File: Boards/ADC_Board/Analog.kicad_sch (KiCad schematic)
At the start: 62 parts, among them J1 Load Cell A, J2 Load Cell B, J3 Load Cell C, J4 Thermocouple A, J5 Cold Juntion Thermistor, J6 Thermocouple A, J7 Thermocouple A, U1 ADS124S08IRHBR

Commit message: Somewhat done servo+adc boards
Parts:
- added C27, C31, C35: 100n, symbol Device:C
- added J15, J17, J19: MIPA_A, symbol Connector_Generic:Conn_01x03
- added R28, R34, R39: 2K, symbol Device:R
- C17: renamed from C3; value XX -> 100n
- C19: renamed from C1; value C -> 200n
- C20: renamed from C4; value XX -> 100n
- C21: renamed from C5; value XX -> 100n
- C22: renamed from C2; value C -> 200n
- C23: renamed from C16; value XX -> 100n
- C24: renamed from C17; value XX -> 100n
- C25: renamed from C22; value C -> 200n
- C26: renamed from C21; value XX -> 100n
- C28: renamed from C23; value XX -> 100n
- C29: renamed from C25; value C -> 200n
- C30: renamed from C24; value XX -> 100n
- C32: renamed from C26; value XX -> 100n
- C33: renamed from C28; value C -> 200n
- C34: renamed from C27; value XX -> 100n
- C36: renamed from C30; value XX -> 100n
- C37: renamed from C32; value C -> 200n
- C38: renamed from C31; value XX -> 100n
- C39: renamed from C36; value XX -> 100n
- C40: renamed from C38; value C -> 200n
- C41: renamed from C37; value XX -> 100n
- C42: renamed from C29; value C -> 100n
- J20: renamed from J6; value Thermocouple A -> Thermocouple B
- J21: renamed from J7; value Thermocouple A -> Thermocouple C
- R18: renamed from R1; value R -> 2K
- R19: renamed from R2; value R -> 2K
- R20: renamed from R3; value R -> 2K
- R22: renamed from R4; value R -> 2K
- R24: renamed from R5; value R -> 2K
- R27: renamed from R11; value R -> 2K
- R30: renamed from R13; value R -> 2K
- R33: renamed from R14; value R -> 2K
- R36: renamed from R15; value R -> 2K
- R37: renamed from R16; value R -> 2K
- R41: renamed from R21; value R -> 2K
- R42: renamed from R22; value R -> 2K
- R46: renamed from R26; value R -> 2K
- R47: renamed from R20; value R -> 2K
- R48: renamed from R33; value R -> 2K
- renumbered C33 to C15, C34 to C16, C35 to C18, J1 to J13, J2 to J14, J3 to J16, J4 to J18, J5 to J22, R25 to R21, R27 to R23, R28 to R25, R29 to R26, R30 to R29, R17 to R35, R18 to R38, R23 to R40, R24 to R43, R34 to R44, R19 to R45, R35 to R49, U1 to U5
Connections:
- net +5V: now also J15.3 (Pin_3), J17.3 (Pin_3), J19.3 (Pin_3)
- net GND: now also C27.2, C31.2, C35.2, J15.1 (Pin_1), J17.1 (Pin_1), J19.1 (Pin_1)
- new net: J17.2 (Pin_2), R34.1
- new net: J19.2 (Pin_2), R39.1
- new net: J15.2 (Pin_2), R28.1
- new net MIPA_A: C27.1, R28.2
- new net MIPA_B: C31.1, R34.2
- new net MIPA_C: C35.1, R39.2
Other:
- note added: "Filters have a -3dB point at 800Hz"
- note added: "MIPA Pres Sensors"

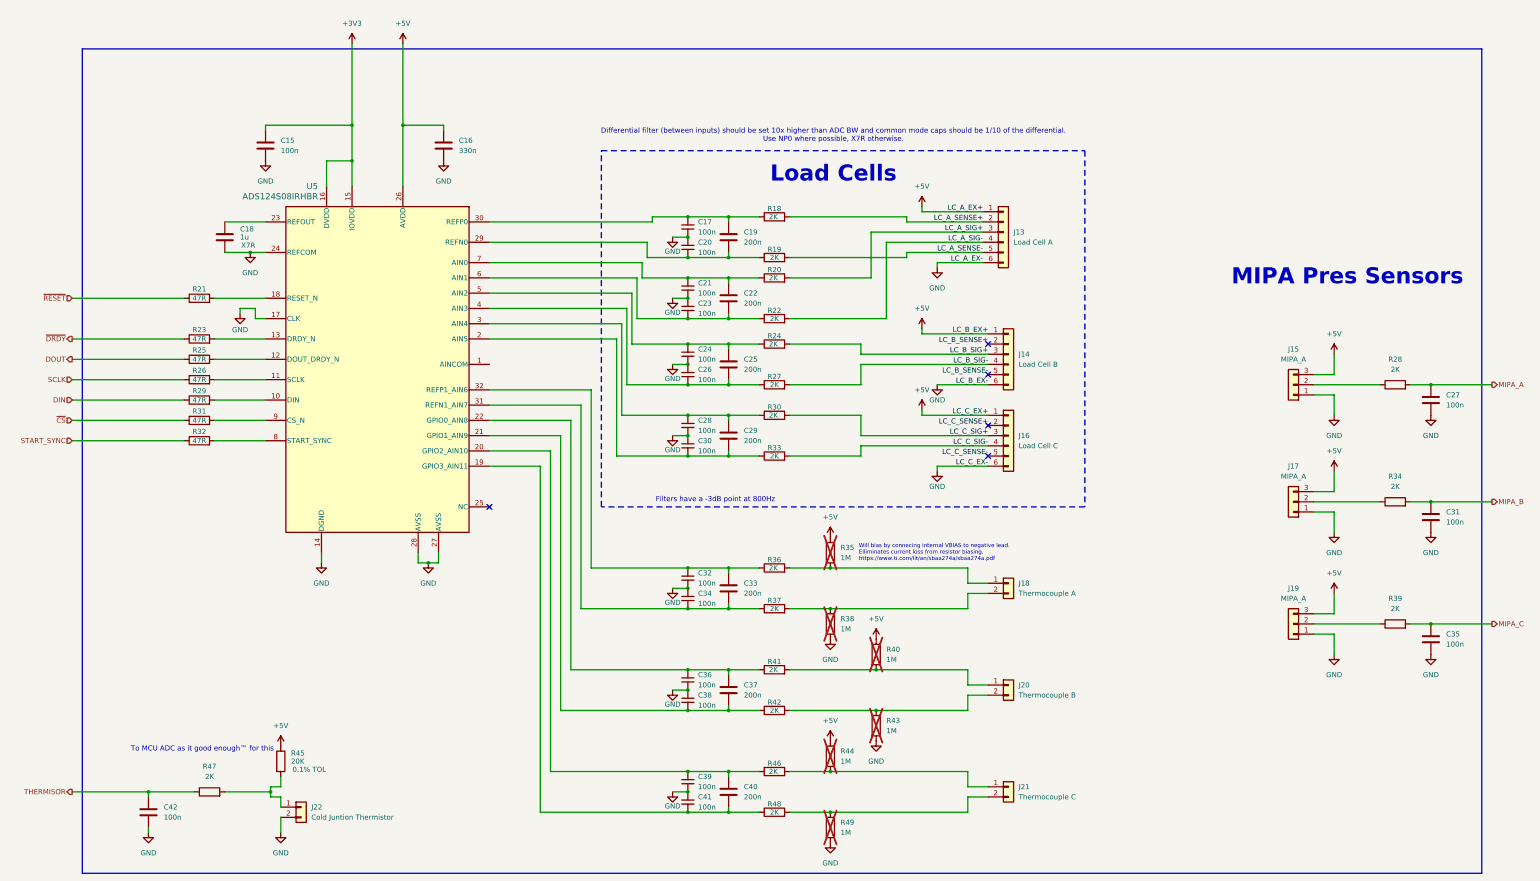
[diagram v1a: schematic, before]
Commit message: Fixes and footprints
Just thermocouples todo
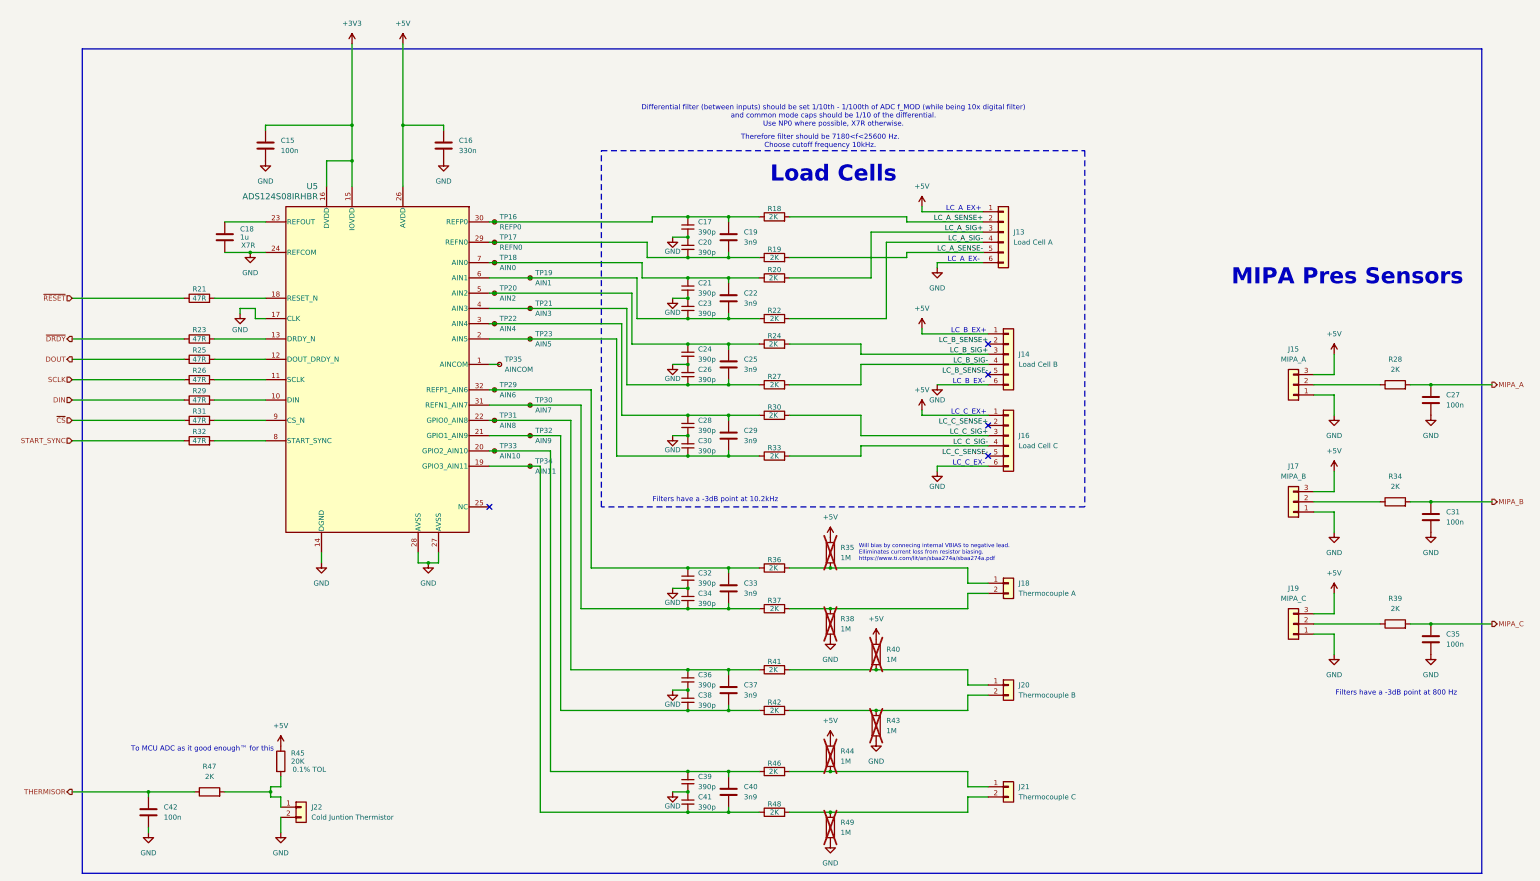
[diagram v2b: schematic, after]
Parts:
- added TP16: REFP0, TestPoint:TestPoint_Pad_1.5x1.5mm, symbol Connector:TestPoint_Small
- added TP17: REFN0, TestPoint:TestPoint_Pad_1.5x1.5mm, symbol Connector:TestPoint_Small
- added TP18: AIN0, TestPoint:TestPoint_Pad_1.5x1.5mm, symbol Connector:TestPoint_Small
- added TP19: AIN1, TestPoint:TestPoint_Pad_1.5x1.5mm, symbol Connector:TestPoint_Small
- added TP20: AIN2, TestPoint:TestPoint_Pad_1.5x1.5mm, symbol Connector:TestPoint_Small
- added TP21: AIN3, TestPoint:TestPoint_Pad_1.5x1.5mm, symbol Connector:TestPoint_Small
- added TP22: AIN4, TestPoint:TestPoint_Pad_1.5x1.5mm, symbol Connector:TestPoint_Small
- added TP23: AIN5, TestPoint:TestPoint_Pad_1.5x1.5mm, symbol Connector:TestPoint_Small
- added TP29: AIN6, TestPoint:TestPoint_Pad_1.5x1.5mm, symbol Connector:TestPoint_Small
- added TP30: AIN7, TestPoint:TestPoint_Pad_1.5x1.5mm, symbol Connector:TestPoint_Small
- added TP31: AIN8, TestPoint:TestPoint_Pad_1.5x1.5mm, symbol Connector:TestPoint_Small
- added TP32: AIN9, TestPoint:TestPoint_Pad_1.5x1.5mm, symbol Connector:TestPoint_Small
- added TP33: AIN10, TestPoint:TestPoint_Pad_1.5x1.5mm, symbol Connector:TestPoint_Small
- added TP34: AIN11, TestPoint:TestPoint_Pad_1.5x1.5mm, symbol Connector:TestPoint_Small
- added TP35: AINCOM, TestPoint:TestPoint_Pad_1.5x1.5mm, symbol Connector:TestPoint_Small
- C15, C16, C18, C27, C31, C35, C42: footprint (none) -> Capacitor_SMD:C_0603_1608Metric
- C17, C20, C21, C23, C24, C26, C28, C30, C32, C34, C36, C38, C39, C41: value 100n -> 390p; footprint (none) -> Capacitor_SMD:C_0603_1608Metric
- C19, C22, C25, C29, C33, C37, C40: value 200n -> 3n9; footprint (none) -> Capacitor_SMD:C_0603_1608Metric
- J13, J14, J16: footprint (none) -> Connector_JST:JST_PH_B6B-PH-K_1x06_P2.00mm_Vertical
- J15: footprint (none) -> Connector_JST:JST_PH_B3B-PH-K_1x03_P2.00mm_Vertical
- J17: value MIPA_A -> MIPA_B; footprint (none) -> Connector_JST:JST_PH_B3B-PH-K_1x03_P2.00mm_Vertical
- J19: value MIPA_A -> MIPA_C; footprint (none) -> Connector_JST:JST_PH_B3B-PH-K_1x03_P2.00mm_Vertical
- J22: footprint (none) -> Connector_JST:JST_PH_B2B-PH-K_1x02_P2.00mm_Vertical
- R18, R19, R20, R21, R22, R23, R24, R25, R26, R27, R28, R29, R30, R31, R32, R33, R34, R35, R36, R37, R38, R39, R40, R41, R42, R43, R44, R45, R46, R47, R48, R49: footprint (none) -> Resistor_SMD:R_0603_1608Metric
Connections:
- net at U5.1 (AINCOM): now also TP35.1
- net at C40.2, C41.2, R48.1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: now also TP34.1
- net at C29.2, C30.2, R33.1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: now also TP23.1
- net at C39.1, C40.1, R46.1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: now also TP33.1
- net at C37.2, C38.2, R42.1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: now also TP32.1
- net at C36.1, C37.1, R41.1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: now also TP31.1
- net at C19.2, C20.2, R19.1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: now also TP17.1
- net at C28.1, C29.1, R30.1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: now also TP22.1
- net at C17.1, C19.1, R18.1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: now also TP16.1
- net at C33.2, C34.2, R37.1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: now also TP30.1
- net at C32.1, C33.1, R36.1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: now also TP29.1
- net at C25.2, C26.2, R27.1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: now also TP21.1
- net at C24.1, C25.1, R24.1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: now also TP20.1
- net at C22.2, C23.2, R22.1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: now also TP19.1
- net at C21.1, C22.1, R20.1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: now also TP18.1
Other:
- note added: "Differential filter (between inputs) should be set 1/10th - 1/100th of ADC f_MOD (while being 10x digital filter) and common mode caps should be 1/10 of the differential. Use NP0 where possible, X7R otherwise."
- note added: "Filters have a -3dB point at 10.2kHz"
- note added: "Filters have a -3dB point at 800 Hz"
- note added: "LC_A_EX+"
- note added: "LC_A_EX-"
- note added: "LC_B_EX+"
- note added: "LC_B_EX-"
- note added: "LC_C_EX+"
- note added: "LC_C_EX-"
- note added: "Therefore filter should be 7180<f<25600 Hz. Choose cutoff frequency 10kHz."
- note removed: "Differential filter (between inputs) should be set 10x higher than ADC BW and common mode caps should be 1/10 of the differential. Use NP0 where possible, X7R otherwise."
- note removed: "Filters have a -3dB point at 800Hz"

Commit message: Selected thermocouple connector, added ferrite bead
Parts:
- added C43: 10u, Capacitor_SMD:C_0603_1608Metric, symbol Device:C
- added FB1: FerriteBead, Inductor_SMD:L_1206_3216Metric, symbol Device:FerriteBead
- added R50: 2R, symbol Device:R
- J18, J20, J21: footprint (none) -> Connector_JST:JST_PH_B2B-PH-K_1x02_P2.00mm_Vertical
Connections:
- net +5V: now also FB1.1; no longer C16.1, J13.1 (Pin_1), J14.1 (Pin_1), J16.1 (Pin_1), R35.1, R40.1, R44.1, R45.1, U5.26 (AVDD)
- net GND: now also R50.2
- new net: C43.2, R50.1
- new net +5VA: C16.1, C43.1, FB1.2, J13.1 (Pin_1), J14.1 (Pin_1), J16.1 (Pin_1), R45.1, U5.26 (AVDD)
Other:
- note added: "For thermocouples will connect to a XE-1107-001 fascia pannel externally"
